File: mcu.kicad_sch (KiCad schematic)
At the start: 18 parts, among them J1 USB_C_Receptacle_USB2.0_14P, J2 Conn_01x05_Pin, J3 Conn_01x03_Pin, J4 Conn_01x01_Pin, SW1 SW_Push, U3 TPD2EUSB30A, U4 STM32G431CBTx

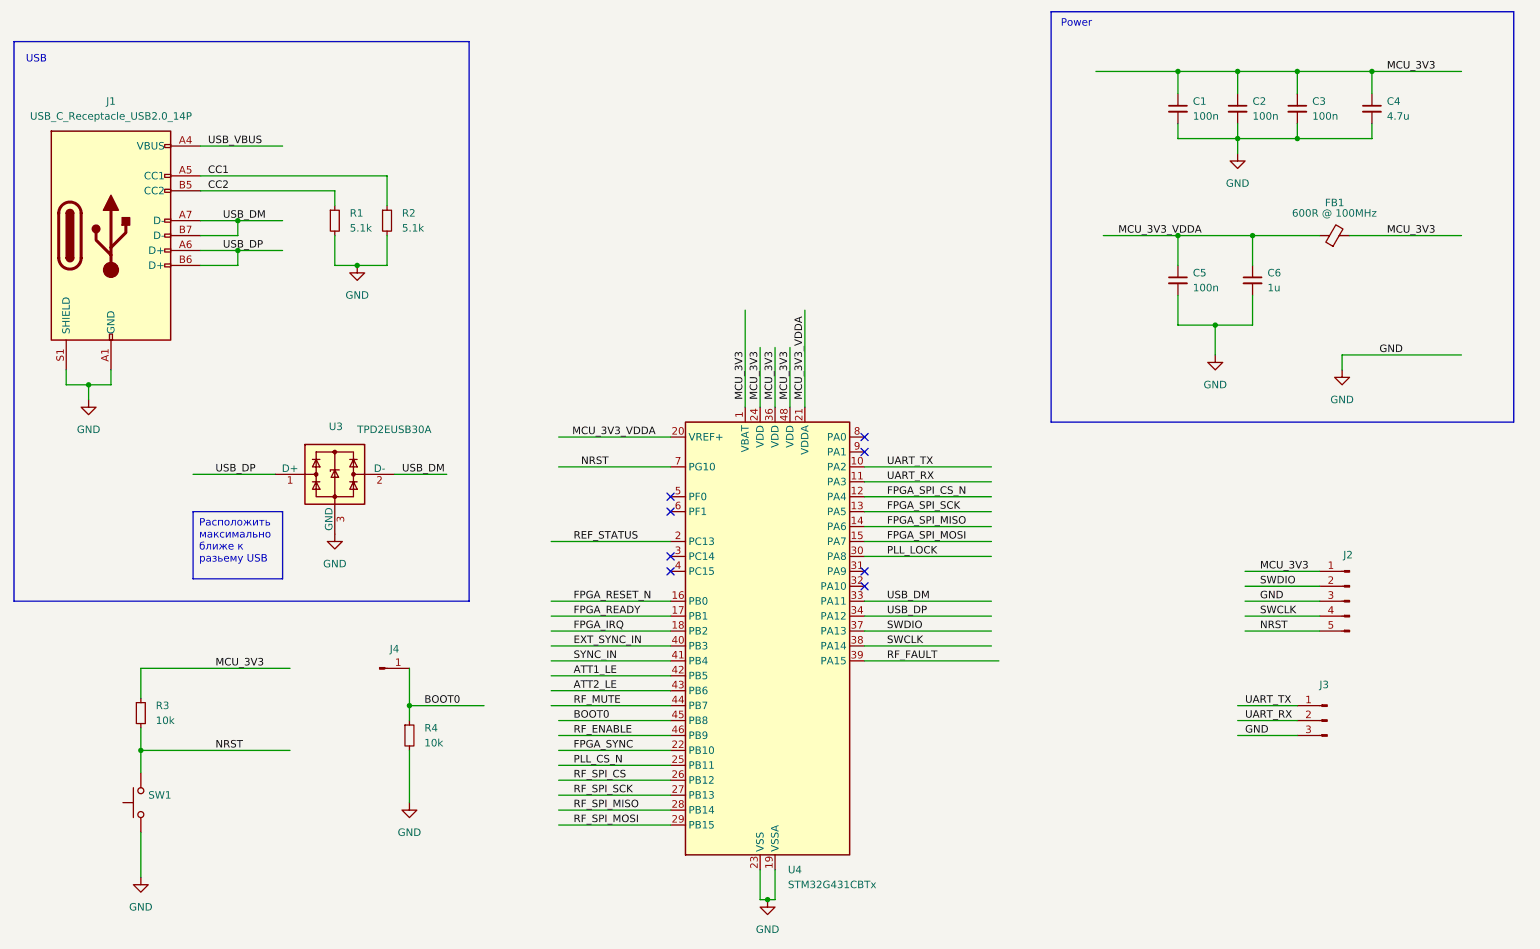
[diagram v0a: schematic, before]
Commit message: Turn to new version Kicad
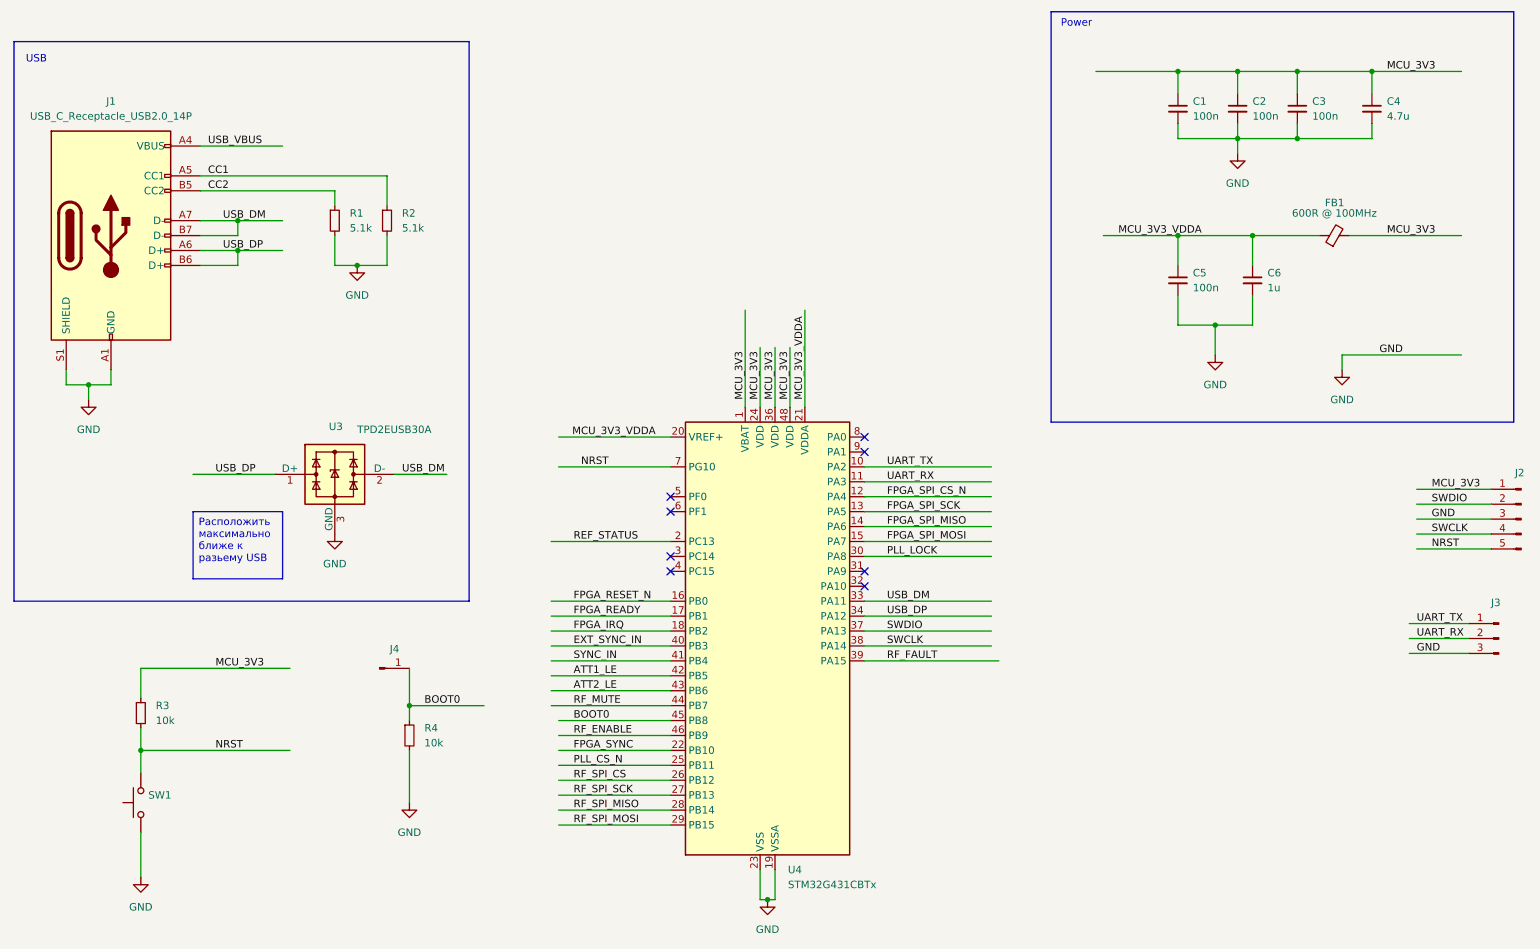
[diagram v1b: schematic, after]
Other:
- moved on the sheet: J2, J3

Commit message: checkpoint: integrate GNSS RF and ADF4351 reference clock
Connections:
- net BOOT0: now also R4.2; no longer R4.1
- net FPGA_SPI_CS_N: now also U4.9 (PA1); no longer U4.12 (PA4)
- net GND: now also R4.1, SW1.2; no longer R4.2, SW1.1
- net NRST: now also SW1.1; no longer SW1.2
- net PLL_CS_N renamed PLL_LE
- net RF_ENABLE renamed MIX_EN
- net RF_MUTE renamed PLL_RF_EN
- new net VCTCXO_CTRL: U4.12 (PA4)
- no-connect marks 8 -> 7
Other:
- moved on the sheet: J4, R3, R4, SW1
